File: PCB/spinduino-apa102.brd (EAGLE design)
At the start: 79.7 x 88.9 mm, 32 parts, among them U1 MC74VHC1GT125DF, U2 MC74VHC1GT125DF

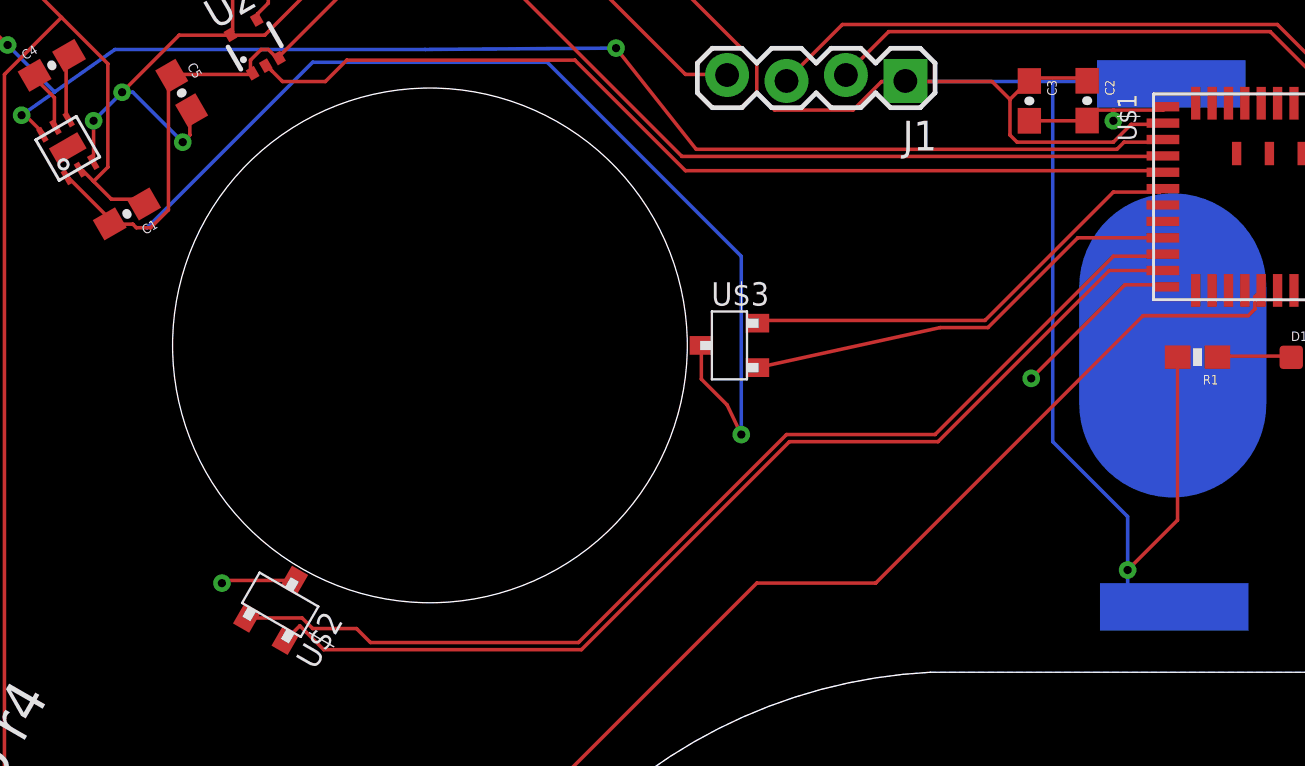
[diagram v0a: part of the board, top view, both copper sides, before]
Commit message: fix: connect one of the hall effect sensors to the 5v power supply
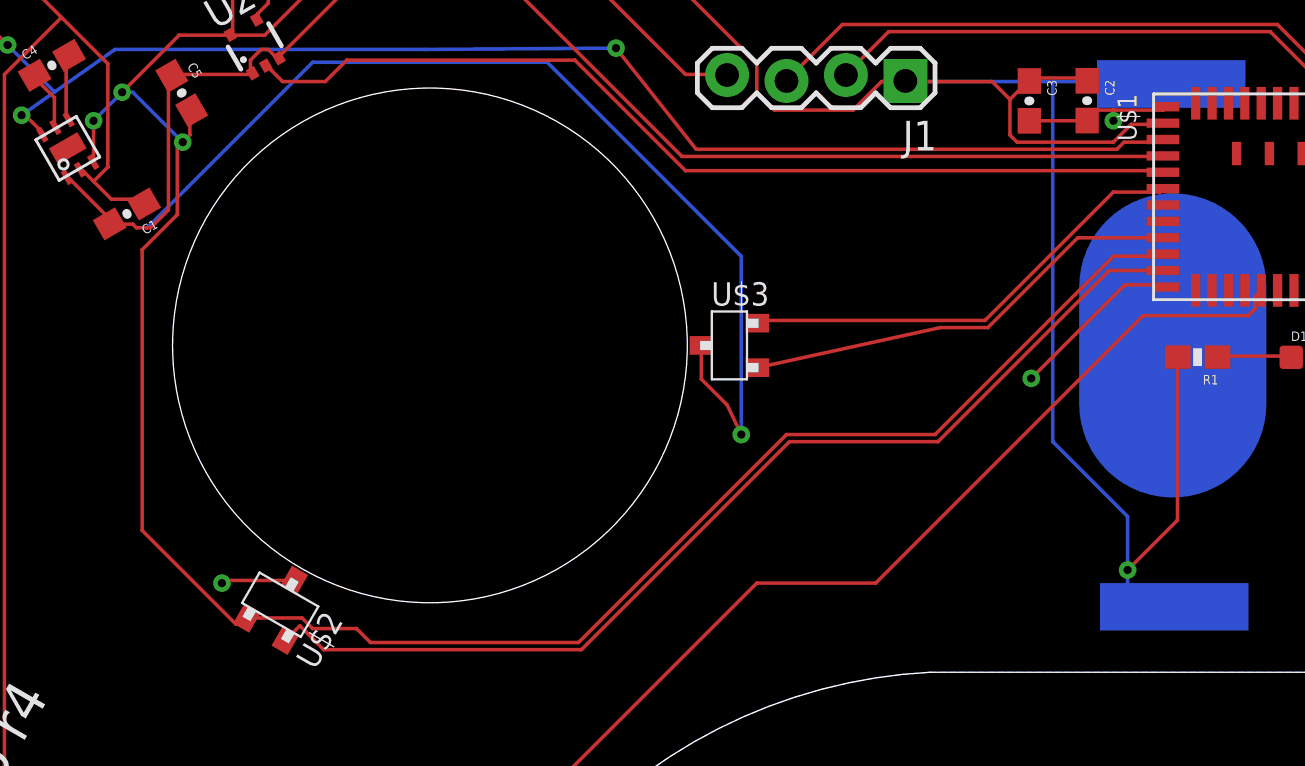
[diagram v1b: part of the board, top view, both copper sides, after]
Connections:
- removed net HALL1PWR: U$1.23, U$2.1
- net 5V: now also U$2.1
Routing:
- net 5V: track 87.9 -> 157.8 mm
- net HALL1PWR: track 46.5 -> 0.00 mm
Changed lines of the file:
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@@
 <wire x1="84.582" y1="41.4528" x2="84.46" y2="41.41" width="0.1524" layer="1"/>
-</signal>
-<signal name="HALL1PWR">
-<contactref element="U$2" pad="1"/>
-<contactref element="U$1" pad="23"/>
-<wire x1="82.13" y1="45.81" x2="82.04" y2="45.72" width="0.1524" layer="1"/>
-<wire x1="82.04" y1="45.72" x2="80.01" y2="45.72" width="0.1524" layer="1"/>
-<wire x1="80.01" y1="45.72" x2="72.39" y2="38.1" width="0.1524" layer="1"/>
-<wire x1="72.39" y1="38.1" x2="66.04" y2="38.1" width="0.1524" layer="1"/>
-<wire x1="66.04" y1="38.1" x2="57.15" y2="29.21" width="0.1524" layer="1"/>
-<wire x1="57.15" y1="29.21" x2="48.26" y2="29.21" width="0.1524" layer="1"/>
-<wire x1="48.26" y1="29.21" x2="47.6622" y2="29.8078" width="0.1524" layer="1"/>
-<wire x1="47.6622" y1="29.8078" x2="45.7871" y2="29.8078" width="0.1524" layer="1"/>
-<wire x1="45.7871" y1="29.8078" x2="45.33425625" y2="30.26064375" width="0.1524" layer="1"/>
-<wire x1="45.33425625" y1="30.26064375" x2="42.977275" y2="30.26064375" width="0.1524" layer="1"/>
 </signal>
 <signal name="HALL2PWR">
@@
 <wire x1="42.3672" y1="60.0456" x2="42.3672" y2="55.3212" width="0.1524" layer="1"/>
 <wire x1="42.3672" y1="55.3212" x2="42.27208125" y2="55.187721875" width="0.1524" layer="1"/>
+<contactref element="U$2" pad="1"/>
+<wire x1="82.04" y1="45.72" x2="80.01" y2="45.72" width="0.1524" layer="1"/>
+<wire x1="80.01" y1="45.72" x2="72.39" y2="38.1" width="0.1524" layer="1"/>
+<wire x1="72.39" y1="38.1" x2="66.04" y2="38.1" width="0.1524" layer="1"/>
+<wire x1="66.04" y1="38.1" x2="57.15" y2="29.21" width="0.1524" layer="1"/>
+<wire x1="57.15" y1="29.21" x2="48.26" y2="29.21" width="0.1524" layer="1"/>
+<wire x1="48.26" y1="29.21" x2="47.6622" y2="29.8078" width="0.1524" layer="1"/>
+<wire x1="47.6622" y1="29.8078" x2="45.7871" y2="29.8078" width="0.1524" layer="1"/>
+<wire x1="45.7871" y1="29.8078" x2="45.33425625" y2="30.26064375" width="0.1524" layer="1"/>
+<wire x1="45.33425625" y1="30.26064375" x2="42.977275" y2="30.26064375" width="0.1524" layer="1"/>
+<wire x1="38.5" y1="34" x2="42.5" y2="30" width="0.1524" layer="1"/>
+<wire x1="38.5" y1="46" x2="38.5" y2="34" width="0.1524" layer="1"/>
+<wire x1="40" y1="47.5" x2="38.5" y2="46" width="0.1524" layer="1"/>
+<wire x1="40" y1="50.5" x2="40" y2="47.5" width="0.1524" layer="1"/>
+<wire x1="42.5" y1="30" x2="42.977275" y2="30.26064375" width="0.1524" layer="1"/>
+<wire x1="40" y1="50.5" x2="40.2336" y2="50.5968" width="0.1524" layer="1"/>
 </signal>
 <signal name="LEDS_ENA">

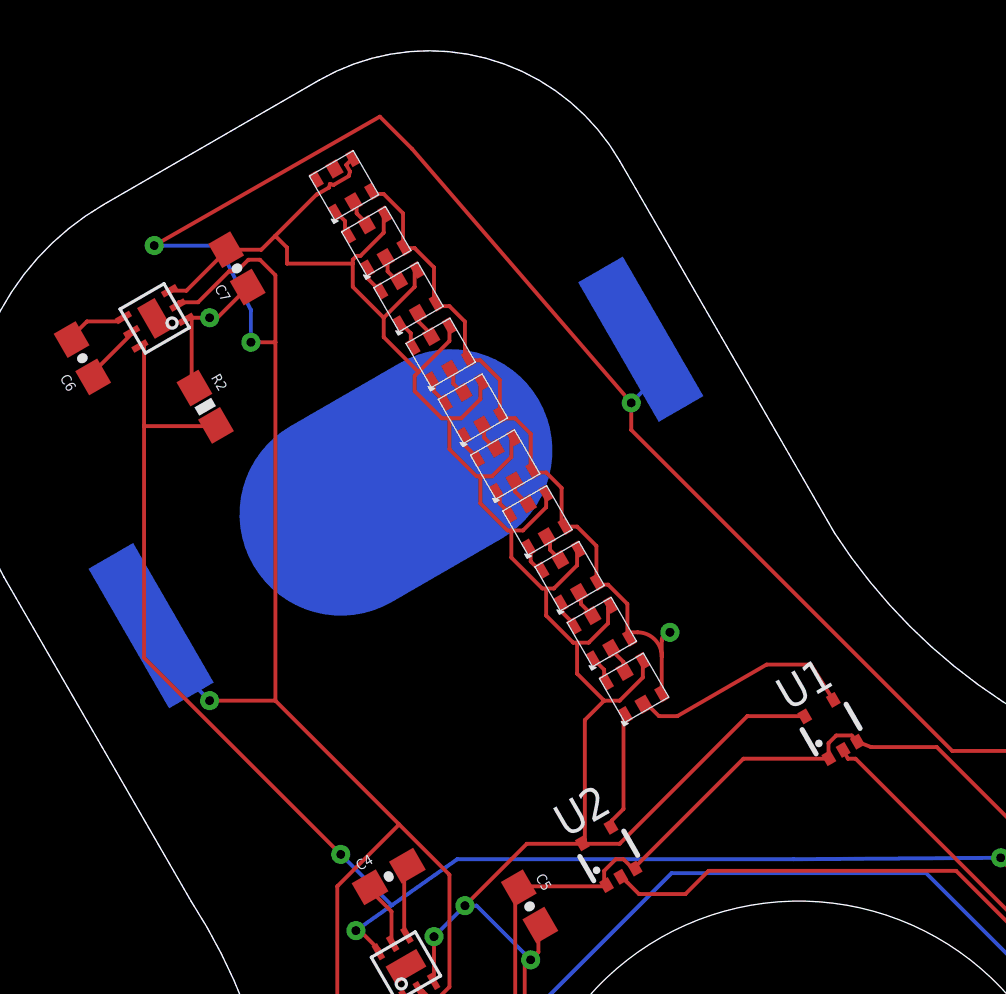
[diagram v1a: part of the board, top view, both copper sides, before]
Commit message: fix: rotate the APA 102 LEDs
So the red / green / blue are aligned (more or less)
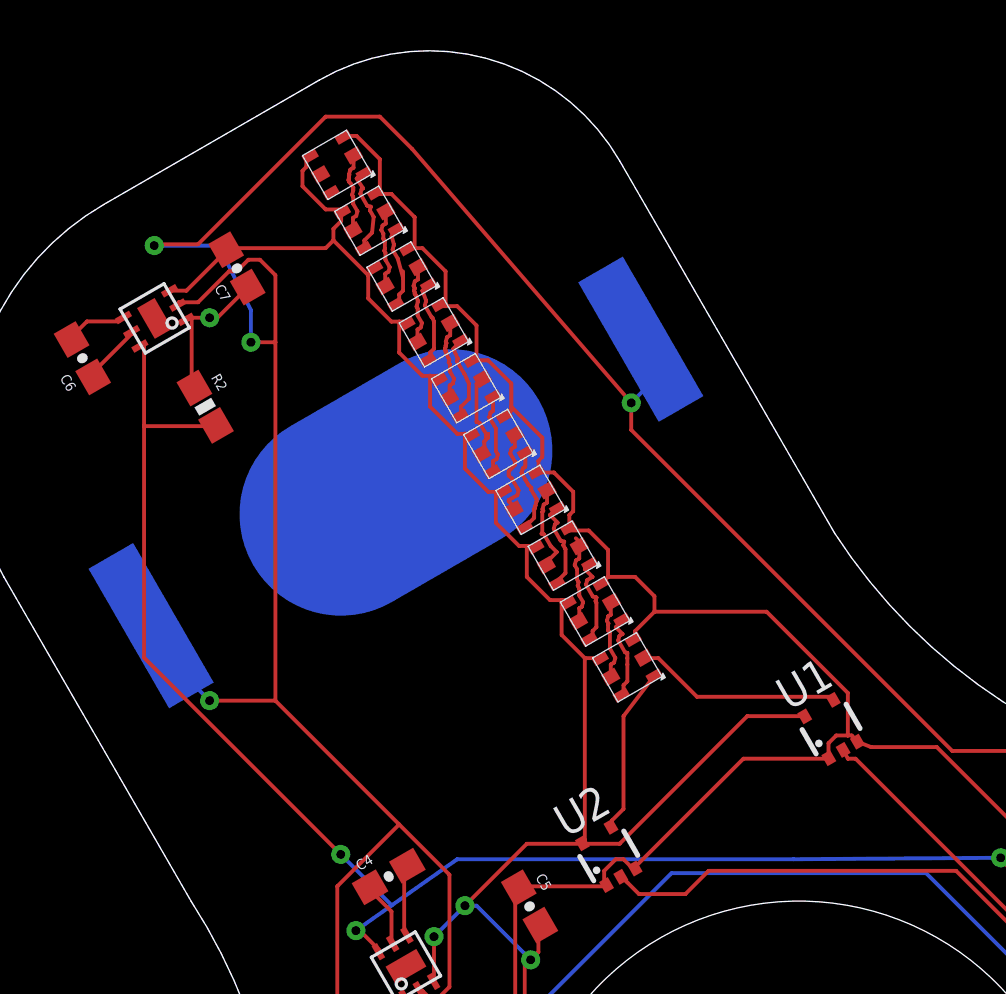
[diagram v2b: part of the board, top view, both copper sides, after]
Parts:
- moved U$13 2.84 mm to (43.1, 65.7), turned to 210 degrees
- moved U$6 2.84 mm to (34.2, 81.1), turned to 210 degrees
- moved U$7 2.84 mm to (35.5, 78.9), turned to 210 degrees
- moved U$10 2.84 mm to (39.3, 72.3), turned to 210 degrees
- moved U$8 2.84 mm to (36.8, 76.7), turned to 210 degrees
- moved U$14 2.84 mm to (44.4, 63.5), turned to 210 degrees
- moved U$11 2.84 mm to (40.6, 70.1), turned to 210 degrees
- moved U$9 2.84 mm to (38.1, 74.5), turned to 210 degrees
- moved U$12 2.84 mm to (41.9, 67.9), turned to 210 degrees
- moved U$5 2.84 mm to (33.0, 83.3), turned to 210 degrees
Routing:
- net 5V: track 157.8 -> 139.2 mm
- net GND: track 142.2 -> 155.6 mm, vias 9 -> 8
- net N$15: track 1.16 -> 3.91 mm
- net N$17: track 1.10 -> 3.67 mm
- net N$1: track 1.12 -> 3.63 mm
- net N$5: track 1.14 -> 3.62 mm
- net N$18: track 1.10 -> 3.58 mm
- net N$14: track 1.15 -> 3.59 mm
- net N$7: track 1.12 -> 3.54 mm
- net N$16: track 1.15 -> 3.52 mm
- net N$19: track 1.15 -> 3.48 mm
- net N$11: track 1.10 -> 3.37 mm
- net N$2: track 1.17 -> 3.37 mm
- net N$6: track 1.10 -> 3.25 mm
- net N$9: track 1.15 -> 3.29 mm
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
